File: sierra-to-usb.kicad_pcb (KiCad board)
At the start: 4 copper layers, 180 x 140 mm, 367 parts, among them CN1 EM92xx / RM520N M.2 Key-B (67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, J1 TYPE-C-31-M-04, J10 BWSMA-KE-Z001, J11 CONMHF4-SMD-G-T, J12 BWSMA-KE-Z001, J13 CONMHF4-SMD-G-T, J14 BWSMA-KE-Z001, J15 CONMHF4-SMD-G-T, J16 BWSMA-KE-Z001, J17 CONMHF4-SMD-G-T, J18 BWSMA-KE-Z001, J2 TYPE-C-31-M-04, J3 TYPE-C-31-M-04, J4 SWD, J5 Qwiic, J6 Fan, J7 Spare, J8 2250504-1, J9 CONMHF4-SMD-G-T, Q1 2N7002, Q2 2N7002, Q20 FDMS86250, Q21 FDMC2523P, Q22 BSC057N08NS3 G, Q23 BSC057N08NS3 G, Q24 FCX493TA, Q25 FCX493TA, Q3 2N7002, Q30 IRLR7843TRPBF, Q31 IRLR7843TRPBF, Q32 DMG3415U-7, Q33 DMG3415U-7, Q34 2N7002, Q35 2N7002, Q36 BSS138, Q37 BSS138, Q38 BSS138, Q39 2N7002, Q4 2N7002, Q40 BSS138, Q5 2N7002, SW1 DIP-4, SW2 LED_KILL, SW3 BOOTSEL, SW4 RUN, T1 750313355, U1 HD3SS3220RNHR, U10 TPS23730RMTR, U11 93C46, U12 TLV62569DBVR, U13 INA226AIDGSR, U14 INA226AIDGSR, U15 TPS62933FDRLR, U17 AP2112K-3.3TRG1, U19 LM5050MKX-1/NOPB, U2 CH224K, U20 TCMT1107, U21 LM5050MKX-1/NOPB, U22 TL431IDBVR, U23 FOD817DS, U24 RP2040, U25 W25Q128JVS, U26 TMP112AIDRLR, U27 TMP112AIDRLR, U28 SK6805-EC15, U29 TS3A27518EPWR, U3 TPS565201DDCR, U30 ST4SIM-200M, U4 AP2112K-3.3TRG1, U5 AP2112K-1.8TRG1, U8 TS3USB221DRCR, U9 RTL8125BG-CG, Y1 12MHz, Y2 25MHz

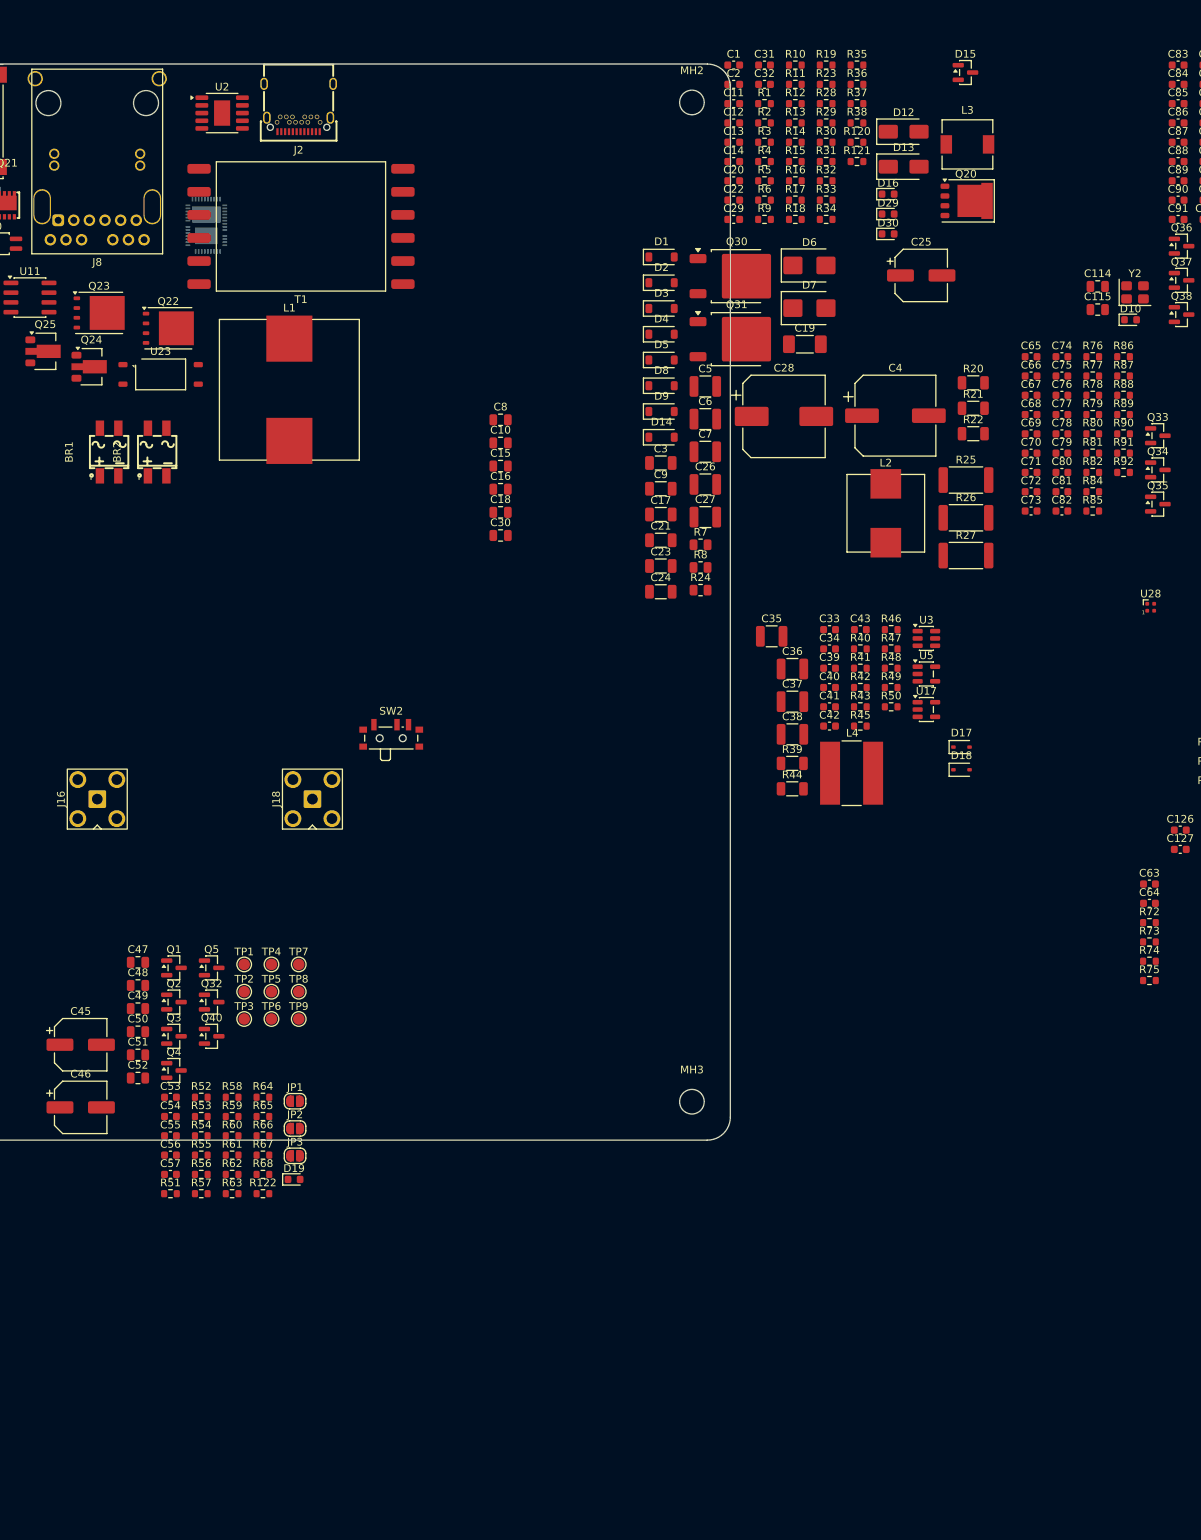
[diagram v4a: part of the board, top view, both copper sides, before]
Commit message: pcb/pro/tools: netclass patterns were dead (hierarchical names) — moat + impedance classes now live, machine-verified
CRITICAL FIX: KiCad netclass patterns match full hierarchical net names.
The Task-15 patterns ('POE_*', 'N_AUX', 'SS_*', 'ANT*'...) only matched
global labels: POE_PRI held just the 4 magjack tap nets (the 54V rail,
POE_VSS, and all control nets were UNPROTECTED by the 2.5mm moat), and
RF_50 matched ZERO nets. Membership now:
- POE_PRI: connectivity-derived (BFS from PoE inputs, stopping at barrier
  parts T1/U20/U23/C19/J8 secondary pins) = 36 primary nets incl. 4 the
  manual Task-15 trace missed (N_CLAMP_D/G, N_AUX_R, N_R43C44), + U10 NC
  pads. POE_STS_RAW (opto-isolated secondary) explicitly excluded — its
  POE_* name had it false-classed, which would have moat-blocked the ADC
  divider route.
- Impedance classes: added */ hierarchical patterns (SS_, PCIE_M/REFCLK,
  MDI, ANT, GNSS); POWER gets */+12V* (flyback secondary).
- Barrier integrity verified: BFS never reaches GND or any rail.
- NEW GATE tools/check_netclasses.py (wired into pre-commit): re-derives
  the primary domain from the netlist and fails on drift/breach.
- Board moat fab-note + .kicad_dru Section-2 comment rewritten to match.
- Parked parts swallowed by the 180x140 resize shifted back off-board
  (39 east +50mm x, 38 south +50mm y).

Real catch now visible: /SIM/UIM2S_IO + UIM2S_CLK tracks run within
2.5mm of U20's primary-side pins (~x93-101,y36-40) — resolve by moving
U20/U23 onto the moat boundary in the PoE corner (planned anyway).

Co-Authored-By: Claude Fable 5 <noreply@anthropic.com>
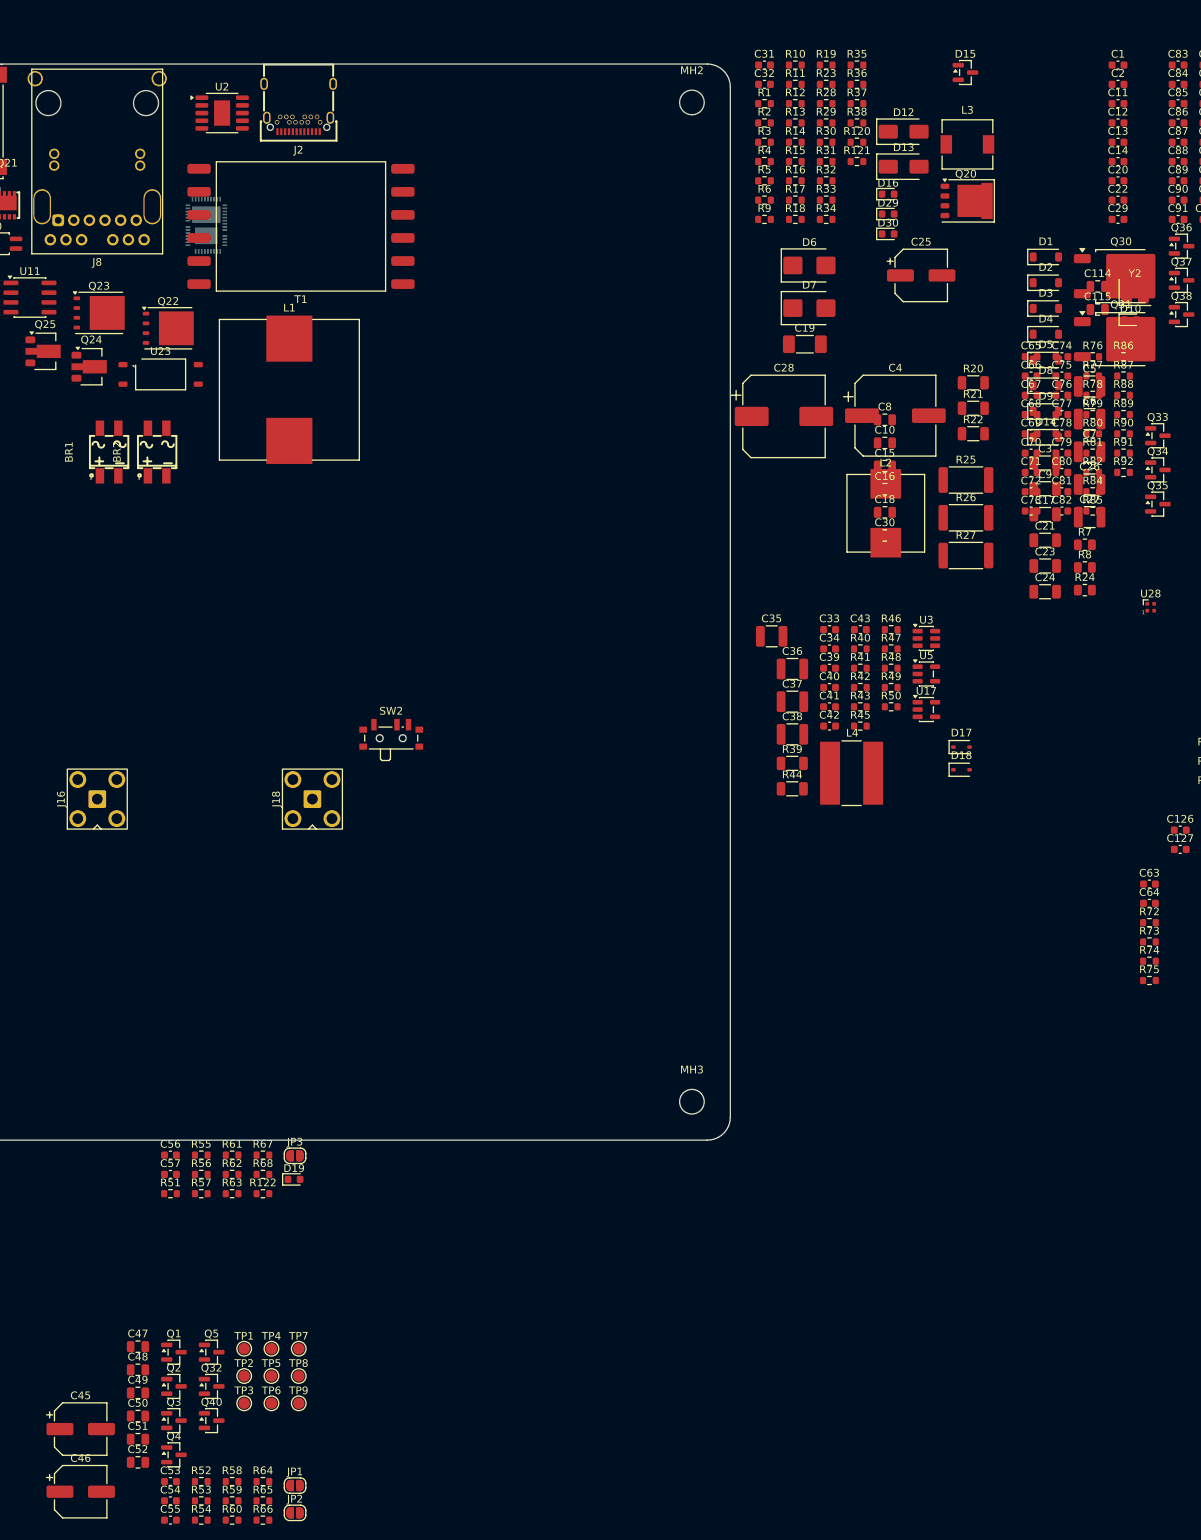
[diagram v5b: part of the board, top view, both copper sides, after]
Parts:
- moved C1 50.0 mm to (247.6, 21.8)
- moved C10 50.0 mm to (217.2, 70.9)
- moved C11 50.0 mm to (247.6, 26.8)
- moved C12 50.0 mm to (247.6, 29.3)
- moved C13 50.0 mm to (247.6, 31.8)
- moved C14 50.0 mm to (247.6, 34.3)
- moved C15 50.0 mm to (217.2, 73.9)
- moved C16 50.0 mm to (217.2, 76.9)
- moved C17 50.0 mm to (238.1, 80.2)
- moved C18 50.0 mm to (217.2, 79.9)
- moved C2 50.0 mm to (247.6, 24.3)
- moved C20 50.0 mm to (247.6, 36.8)
- moved C21 50.0 mm to (238.1, 83.6)
- moved C22 50.0 mm to (247.6, 39.3)
- moved C23 50.0 mm to (238.1, 86.9)
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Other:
- board text added: "POE_PRI_MOAT (placeholder zone, resize to enclose placed primary-side components): Enforces >=2.5mm copper clearance from POE_PRI-netclass copper to all other-net copper (.kicad_dru). POE_PRI membership (2026-07-16, connectivity-derived, machine-verified by tools/check_netclasses.py in the pre-commit hook): POE_VA+/-, POE_VB+/-, and the /Power Input/ locals POE_VDD54, POE_VDD54_F, POE_VSS, POE_RT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"
- board text removed: "POE_PRI_MOAT (placeholder zone, resize to enclose placed primary-side components): Enforces >=2.5mm copper clearance from any POE_PRI-netclass copper to all other-net copper (see .kicad_dru). POE_PRI = POE_VA+/-, POE_VB+/-, POE_VDD54, POE_VDD54_F, POE_VSS, POE_RTN, plus TPS23730/Q20/T1-primary control nets N_AUX,N_BT,N_BTLED,N_CLSA,N_CLSB,N_COMP,N_CS, N_CS_SNS,N_DEN,N_DT,N_DTHR,N_FRS,N_GAT2,N_GAT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"

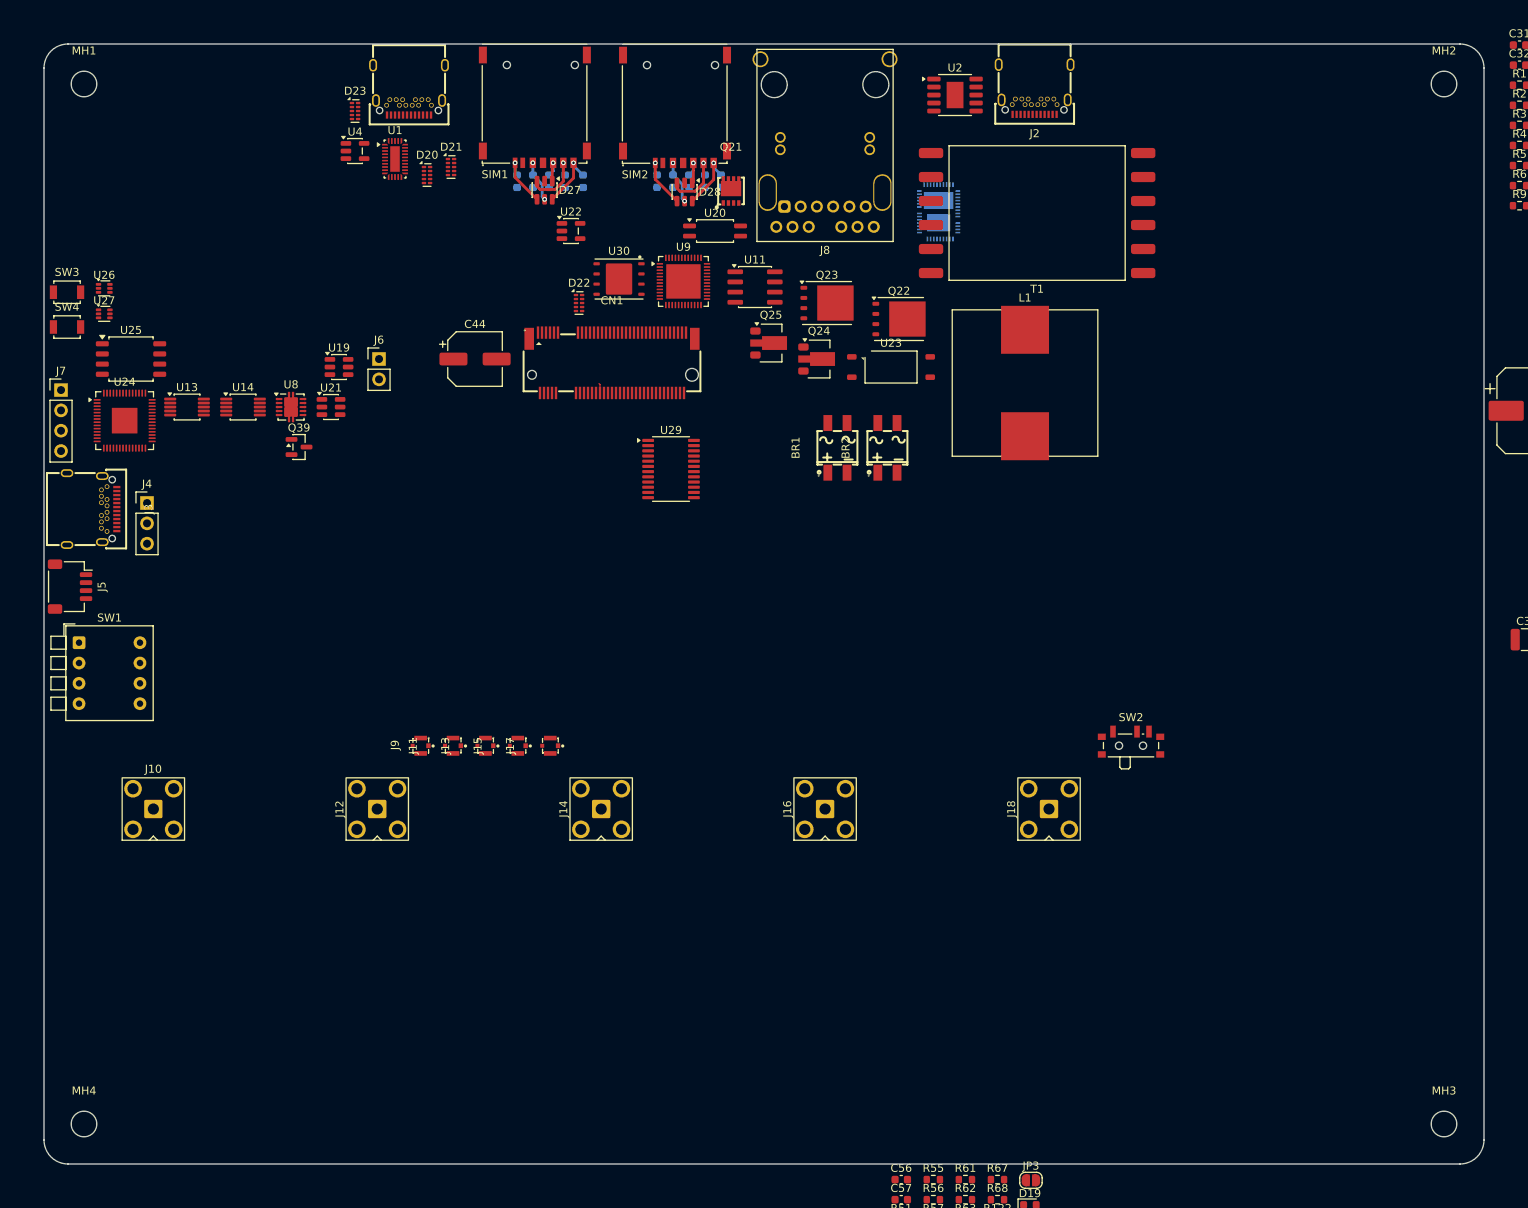
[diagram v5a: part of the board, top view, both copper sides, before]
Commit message: pcb: GND edge border band + via fence (edge-plating-ready cosmetics)
2.0mm GND zones on F.Cu+B.Cu, inset 0.5mm from the outline (8 band
zones, priority 1, unfilled — press B in pcbnew to fill), with a
0.6/0.3 GND via fence at 4mm pitch on the 1.5mm centerline (154 vias;
2 dropped where J2 shield legs / J5 mount pin punch through the band).
No edge plating this rev; if added later the band gives the plating
continuous copper to bond to. NOTE: the band is GND copper at the
edge, so the PoE moat now (correctly) requires primary copper to stay
>=2.5mm inboard of it (~5mm from the board edge) — same constraint
edge plating would impose. Fence vias near re-placed edge connectors
may need manual nudging after final placement.

Co-Authored-By: Claude Fable 5 <noreply@anthropic.com>
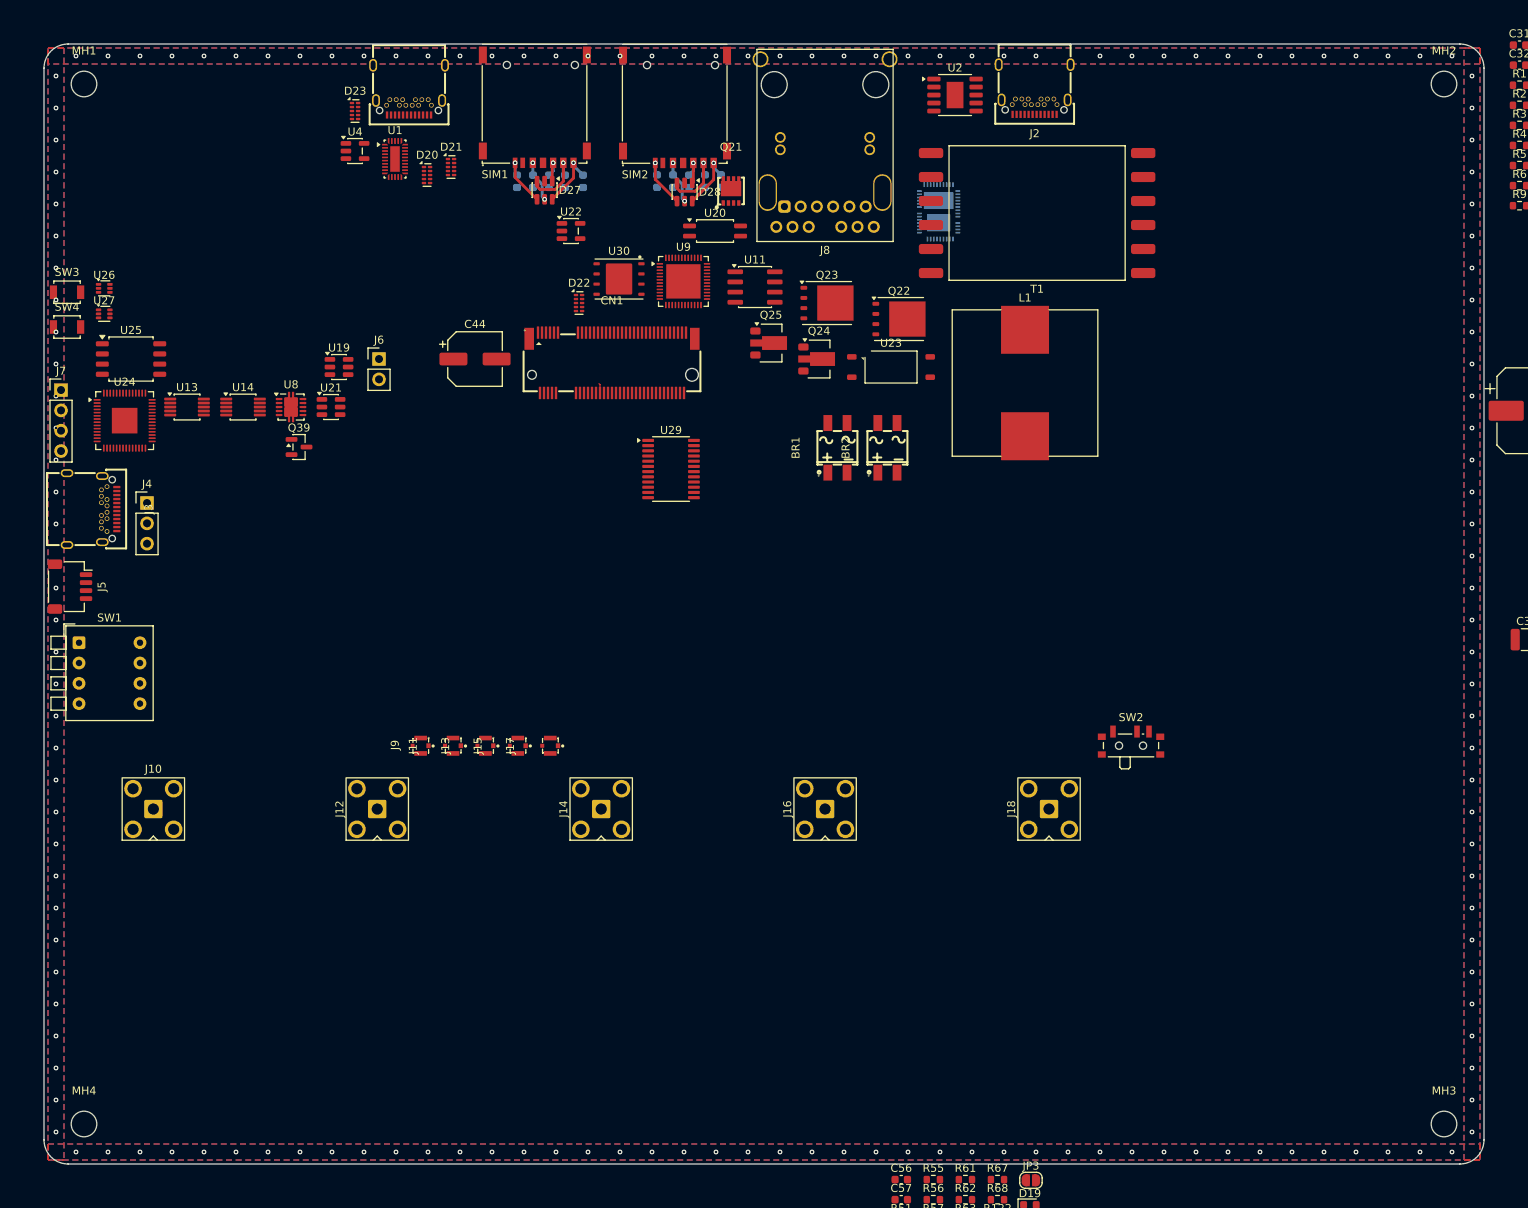
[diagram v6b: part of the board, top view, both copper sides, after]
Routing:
- net GND: vias 0 -> 154
- added copper zone on B.Cu, net GND
- added copper zone on F.Cu, net GND

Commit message: pcb: layout progress snapshot (user session)
Co-Authored-By: Claude Fable 5 <noreply@anthropic.com>
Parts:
- moved J5 0.13 mm to (20.5, 89.5)
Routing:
- net GND: vias 154 -> 150
- net /MCU/RP2040_RUN: vias 0 -> 1
- net /MCU/QSPI_SS: vias 0 -> 1
- net /MCU/MCU_GPIO24: vias 0 -> 1
- net +3V3_MCU: vias 0 -> 1
